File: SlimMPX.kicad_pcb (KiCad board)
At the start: 2 copper layers, 16 x 14 mm, 2 parts

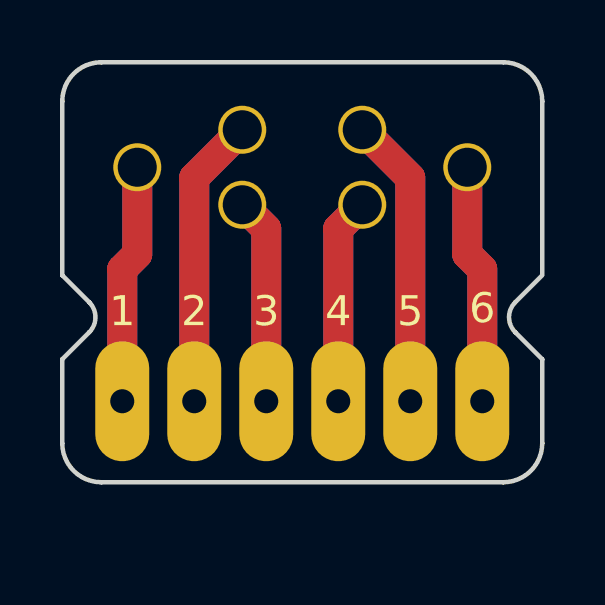
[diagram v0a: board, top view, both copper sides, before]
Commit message: Version 2 Vias are now covered by soldermask, outside the pad, so to avoid solder flowing to the other side when soldering.
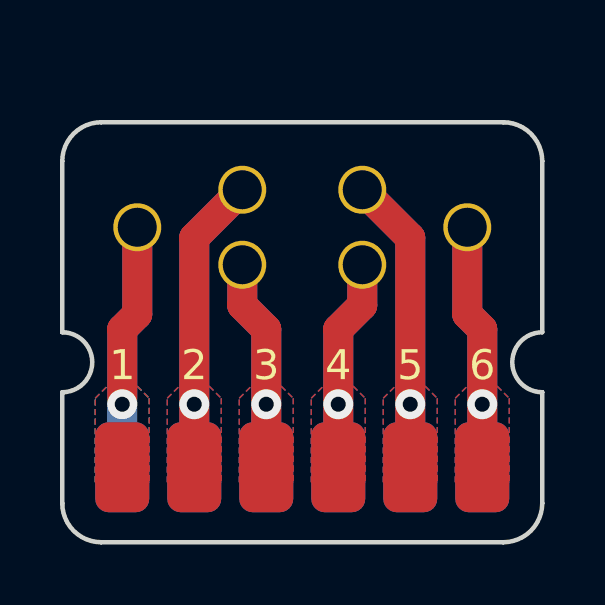
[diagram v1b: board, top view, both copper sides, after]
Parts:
- removed REF**: Output_MPX, myfootprint:Output_MPX
- removed REF**: MPX Connector, myfootprint:MPX Connector
- added J1: Conn_01x06, myfootprint:MPX_Connector, F.Cu at (108.0, 105.5)
- added J2: Conn_01x06, myfootprint:Output_MPX, F.Cu at (108.0, 113.5)
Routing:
- net (no net): track 103.8 -> 0.00 mm
- net Net-(J1-Pad5): track 0.00 -> 20.3 mm, vias 0 -> 1
- net Net-(J1-Pad2): track 0.00 -> 20.3 mm, vias 0 -> 1
- net Net-(J1-Pad6): track 0.00 -> 16.9 mm, vias 0 -> 1
- net Net-(J1-Pad4): track 0.00 -> 14.7 mm, vias 0 -> 1
- net Net-(J1-Pad3): track 0.00 -> 14.7 mm, vias 0 -> 1
- net Net-(J1-Pad1): track 0.00 -> 14.4 mm, vias 0 -> 1
- added copper zone on B.Cu, net (none)
- added copper zone on B.Cu, net Net-(J1-Pad1)
- added copper zone on F.Cu, net Net-(J1-Pad1)
- added copper zone on B.Cu, net Net-(J1-Pad2)
- added copper zone on F.Cu, net Net-(J1-Pad2)
- added copper zone on B.Cu, net Net-(J1-Pad3)
- added copper zone on F.Cu, net Net-(J1-Pad3)
- added copper zone on B.Cu, net Net-(J1-Pad4)
- added copper zone on F.Cu, net Net-(J1-Pad4)
- added copper zone on B.Cu, net Net-(J1-Pad5)
- added copper zone on F.Cu, net Net-(J1-Pad5)
- added copper zone on B.Cu, net Net-(J1-Pad6)
- added copper zone on F.Cu, net Net-(J1-Pad6)
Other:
- outline, holes or cut-outs redrawn
